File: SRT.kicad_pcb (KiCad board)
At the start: 2 copper layers, 346.6 x 347.7 mm, 302 parts, among them J1 PreampOut, J2 In, J3 Send, J4 Return, J7 LineOut, J8 Cab/Phones, J9 Footswitch, K1 CR/LD, K2 CL/DR, K3 CL/DR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

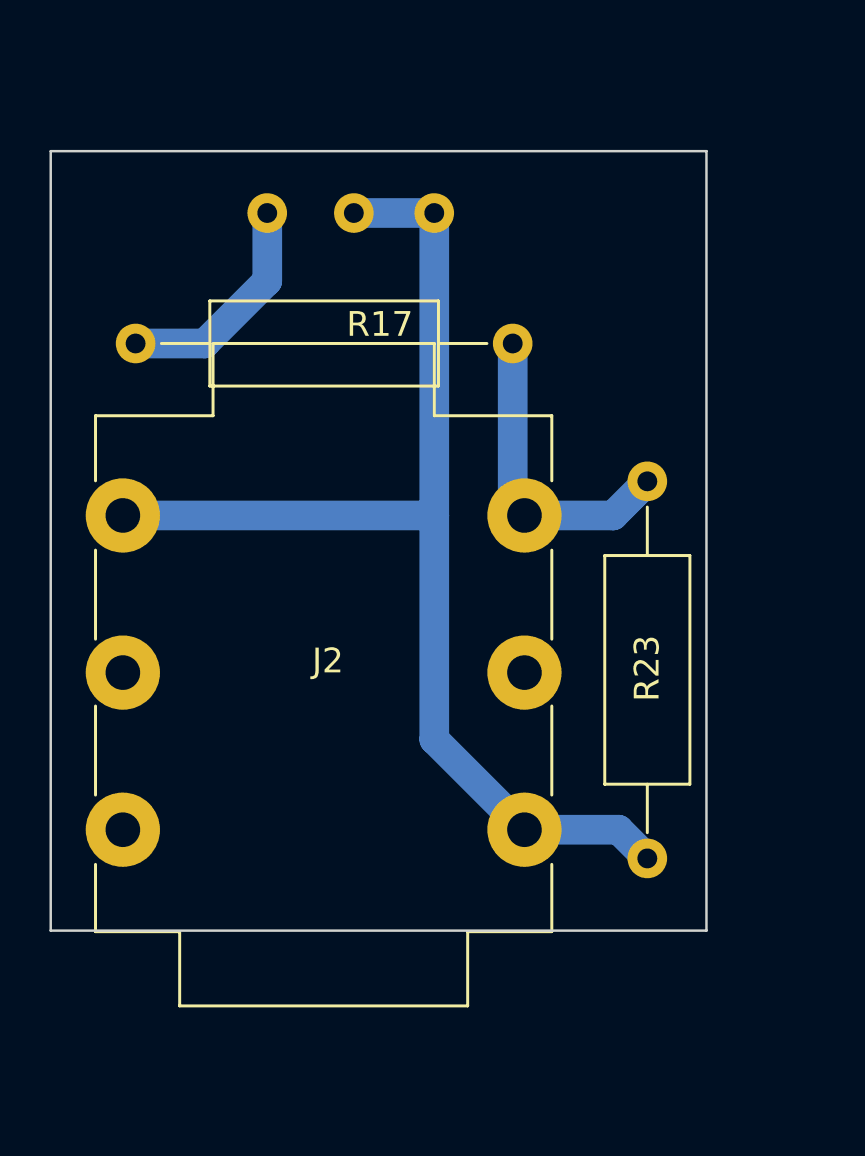
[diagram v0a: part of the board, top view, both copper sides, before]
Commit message: Изменён формат 3D моделей после обновления версии Kicad
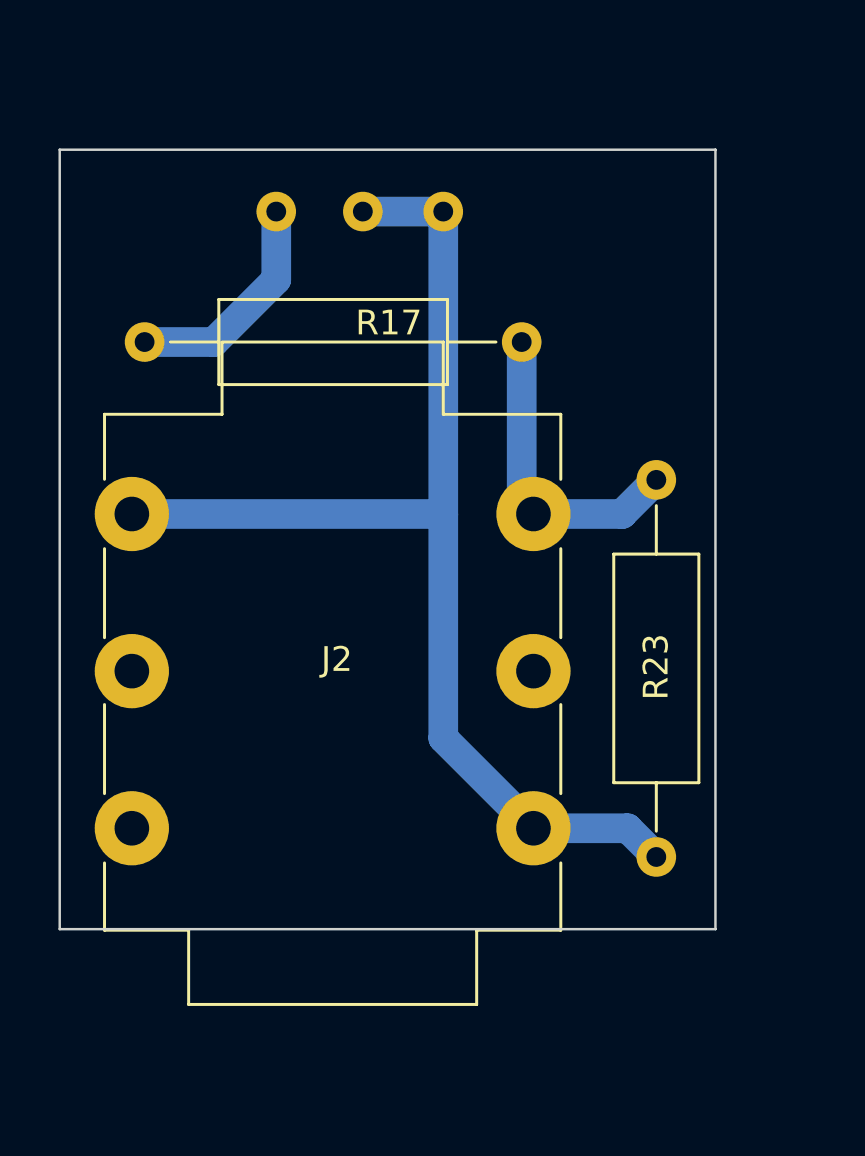
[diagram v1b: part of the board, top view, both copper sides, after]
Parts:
- moved R17 0.37 mm to (454.7, 436.0)
- moved R23 0.37 mm to (460.1, 456.8)
- moved ? 0.37 mm to (448.2, 430.8)
- moved ? 0.37 mm to (444.8, 430.8)
- moved ? 0.37 mm to (451.5, 430.8)
- moved J2 0.37 mm to (455.1, 443.0)
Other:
- board size 346.6 x 347.7 mm -> 346.2 x 347.7 mm
